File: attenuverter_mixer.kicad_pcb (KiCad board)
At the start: 2 copper layers, 98 parts, among them J0 Eurorack power, J1 Input, J10 Or out, J2 Out, J3 Input, J4 Out, J5 Input, J6 Input, J7 Out, J8 Out, J9 Sum out, U1 TL072, U2 TL072, U3 TL072, U4 TL072, U5 TL074, U6 LM4040CIZ-5.0

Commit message: Where it's at, just before changing the op amp configuration
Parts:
- removed D5, D6: D_TVS, Diode_THT:D_DO-15_P12.70mm_Horizontal
- removed R33, R36, R7, R8: 100R, Resistor_THT:R_Axial_DIN0204_L3.6mm_D1.6mm_P7.62mm_Horizontal
- J1, J10, J2, J3, J4, J5, J6, J7, J8, J9, RV1, RV2, RV3, RV4, RV5, RV6: moved to B.Cu
- R10, R11, R12, R13, R14, R15, R16, R17, R18, R19, R2, R20, R21, R22, R23, R24, R25, R26, R27, R28, R29, R3, R34, R35, R37, R38, R39, R4, R40, R41, R42, R45, R46, R6, R9: footprint Resistor_THT:R_Axial_DIN0207_L6.3mm_D2.5mm_P10.16mm_Horizontal -> Resistor_SMD:R_1206_3216Metric_Pad1.42x1.75mm_HandSolder
- moved J10 187.6 mm to (207.3, 134.9), turned to 270 degrees
- moved J8 184.8 mm to (224.5, 125.7)
- moved RV6 165.0 mm to (210.1, 122.7), turned to 90 degrees
- moved J9 152.4 mm to (190.8, 134.9), turned to 270 degrees
- moved J6 148.6 mm to (186.7, 125.2)
- moved D16 108.5 mm to (146.7, 82.7), turned to 180 degrees
- moved D17 100.8 mm to (130.9, 97.2)
- moved R30 94.9 mm to (153.0, 72.1), turned to 90 degrees
- moved R1 93.6 mm to (143.1, 73.0), turned to 90 degrees
- moved U5 90.7 mm to (168.1, 106.7), turned to 90 degrees
- moved U6 80.2 mm to (149.7, 121.3)
- moved C1 80.1 mm to (138.0, 102.6)
- moved J0 78.2 mm to (102.1, 110.5)
- moved R11 69.0 mm to (158.5, 59.7)
- moved C2 66.7 mm to (143.3, 115.7), turned to 180 degrees
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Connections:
- J0 pad 10: Net-(D16-Pad1) -> Net-(D17-Pad2)
- J0 pad 2: GND -> Net-(D16-Pad1)
- J0 pad 3: GNDPWR -> GND
- J0 pad 5: Net-(D17-Pad2) -> GNDPWR
- J0 pad 6: Net-(D17-Pad2) -> GNDPWR
- J0 pad 8: GNDPWR -> GND
- J0 pad 9: GND -> Net-(D17-Pad2)
- R15 pad 1: Net-(R15-Pad1) -> Net-(J1-PadT)
- R20 pad 2: Net-(R15-Pad1) -> Net-(J1-PadT)
- R21 pad 2: Net-(R21-Pad2) -> Net-(J3-PadT)
- R34 pad 1: Net-(D5-Pad1) -> Net-(J5-PadT)
- R37 pad 1: Net-(D6-Pad1) -> Net-(J6-PadT)
- R39 pad 2: Net-(D5-Pad1) -> Net-(J5-PadT)
- R40 pad 2: Net-(D6-Pad1) -> Net-(J6-PadT)
- R9 pad 1: Net-(R21-Pad2) -> Net-(J3-PadT)
- RV1 pad 1: Net-(R15-Pad1) -> Net-(J1-PadT)
- RV4 pad 1: Net-(R21-Pad2) -> Net-(J3-PadT)
- RV5 pad 1: Net-(D5-Pad1) -> Net-(J5-PadT)
- RV6 pad 1: Net-(D6-Pad1) -> Net-(J6-PadT)

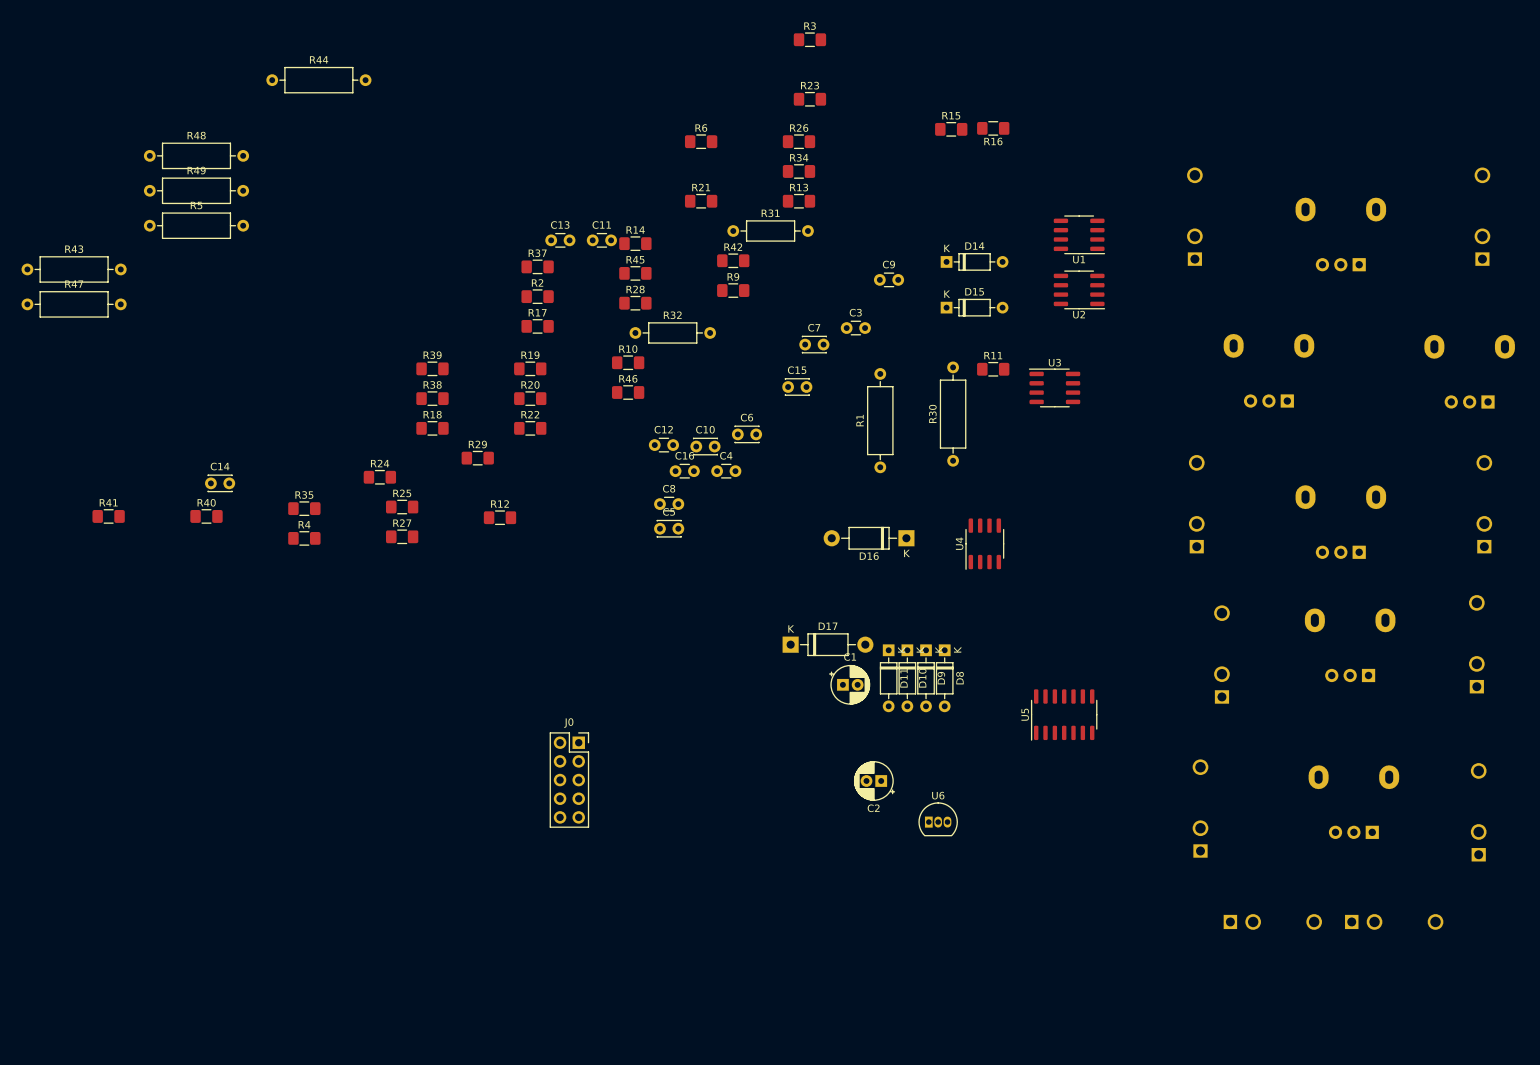
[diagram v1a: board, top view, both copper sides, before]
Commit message: V01 as fabricated
- Use surface mount 100K and 220K to allow single board.
- Drop offset pots --- just have atteunuvert controls on each channel.
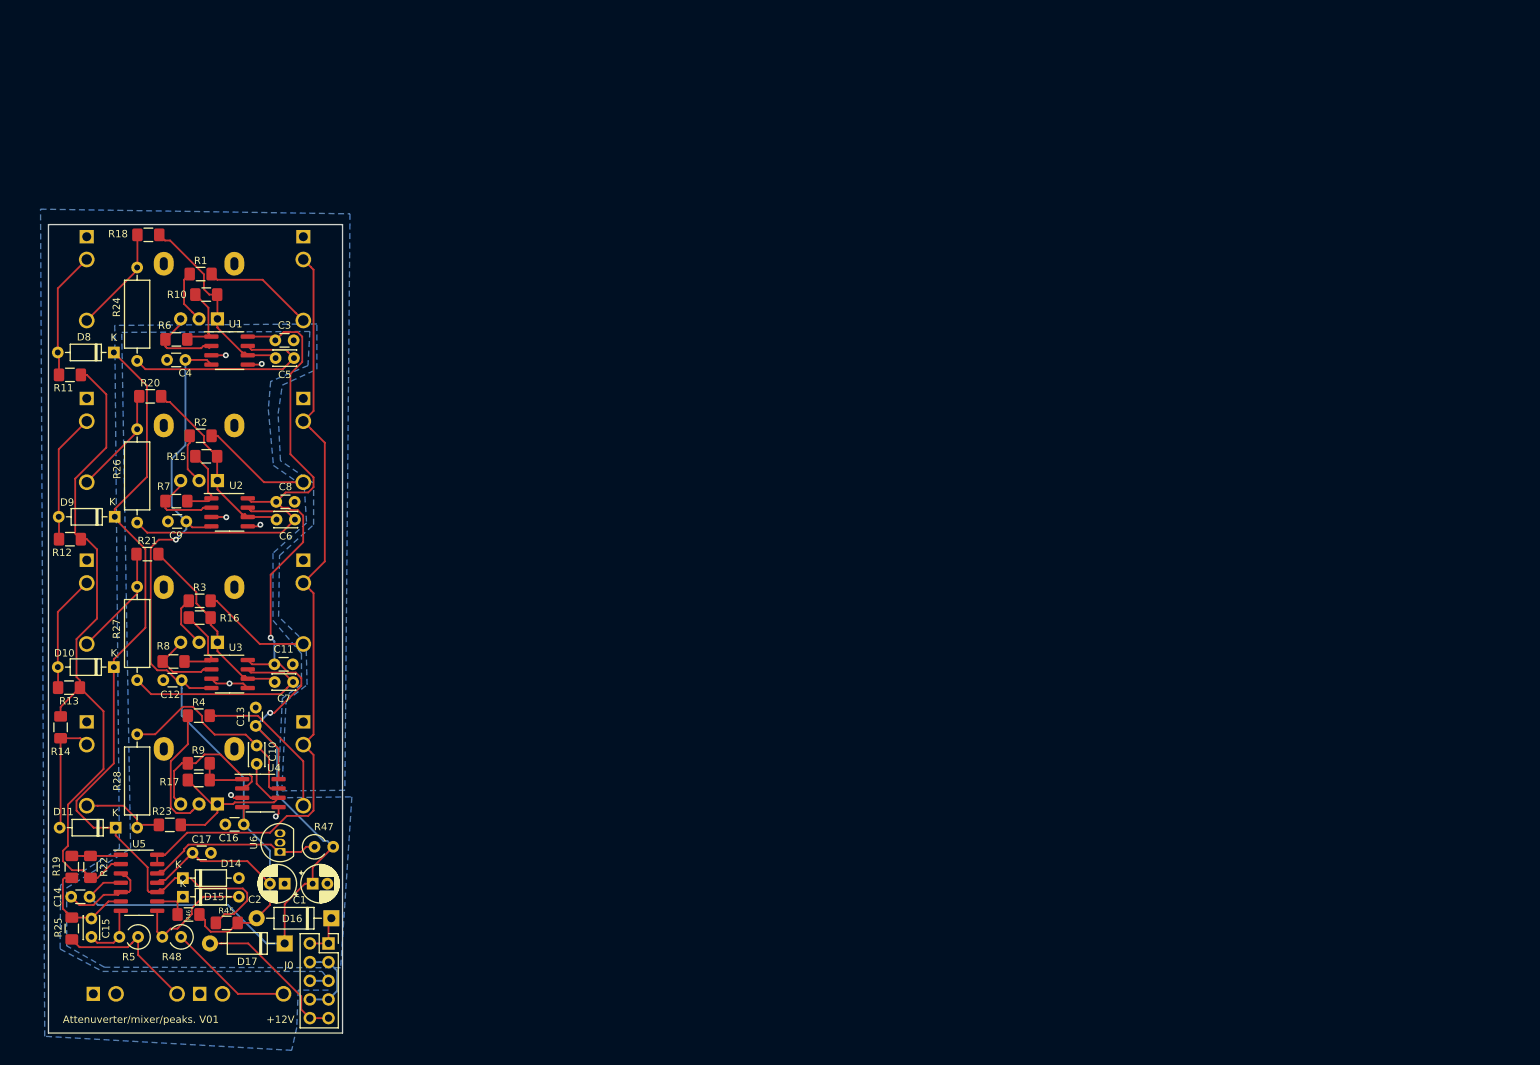
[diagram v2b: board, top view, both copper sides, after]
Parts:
- removed R29, R39, R40, R41, R42: 100k, Resistor_SMD:R_1206_3216Metric_Pad1.42x1.75mm_HandSolder
- removed R30, R43, R44: 330R, Resistor_THT:R_Axial_DIN0309_L9.0mm_D3.2mm_P12.70mm_Horizontal
- removed R31, R32: 100k, Resistor_THT:R_Axial_DIN0207_L6.3mm_D2.5mm_P10.16mm_Horizontal
- removed R34, R35, R37, R38: 47k, Resistor_SMD:R_1206_3216Metric_Pad1.42x1.75mm_HandSolder
- removed R49: R, Resistor_THT:R_Axial_DIN0309_L9.0mm_D3.2mm_P12.70mm_Horizontal
- removed RV5, RV6: 100k, Potentiometer_THT:Potentiometer_Alpha_RD901F-40-00D_Single_Vertical
- added C17: 100nF, Capacitor_THT:C_Disc_D3.0mm_W1.6mm_P2.50mm, F.Cu at (52.1, 125.5)
- added R7: 100k, Resistor_SMD:R_1206_3216Metric_Pad1.42x1.75mm_HandSolder, F.Cu at (47.4, 77.6)
- added R8: 100k, Resistor_SMD:R_1206_3216Metric_Pad1.42x1.75mm_HandSolder, F.Cu at (47.0, 99.4)
- C14: value 18pF -> 100nF; footprint Capacitor_THT:C_Disc_D3.0mm_W2.0mm_P2.50mm -> Capacitor_THT:C_Disc_D3.0mm_W1.6mm_P2.50mm
- J4: value Out -> Input
- J6: value Input -> Out
- R1: value 330R -> 100k; footprint Resistor_THT:R_Axial_DIN0309_L9.0mm_D3.2mm_P12.70mm_Horizontal -> Resistor_SMD:R_1206_3216Metric_Pad1.42x1.75mm_HandSolder
- R10, R15, R16, R9: value 47k -> 100k
- R24, R26, R27, R28: value 100k -> 330R; footprint Resistor_SMD:R_1206_3216Metric_Pad1.42x1.75mm_HandSolder -> Resistor_THT:R_Axial_DIN0309_L9.0mm_D3.2mm_P12.70mm_Horizontal
- R47, R48, R5: footprint Resistor_THT:R_Axial_DIN0309_L9.0mm_D3.2mm_P12.70mm_Horizontal -> Resistor_THT:R_Axial_DIN0309_L9.0mm_D3.2mm_P2.54mm_Vertical
- RV1, RV2, RV3, RV4: value 100k -> 10k
- moved J8 190.2 mm to (35.2, 107.7), turned to 180 degrees
- moved J2 189.9 mm to (35.2, 41.7), turned to 180 degrees
- moved J7 189.9 mm to (35.2, 85.7), turned to 180 degrees
- moved RV3 175.9 mm to (53.0, 96.8)
- moved J6 163.5 mm to (35.2, 63.7), turned to 180 degrees
- moved J4 160.7 mm to (64.6, 85.7), turned to 180 degrees
- moved RV4 159.1 mm to (53.0, 118.8)
- moved J10 157.0 mm to (50.5, 144.7)
- moved RV1 155.5 mm to (53.0, 52.8)
- moved J9 155.0 mm to (36.1, 144.7)
- moved RV2 145.9 mm to (53.0, 74.8)
- moved D14 133.5 mm to (48.3, 128.9)
- moved R23 131.6 mm to (46.5, 121.7)
- moved D15 131.2 mm to (48.3, 131.4)
- moved U5 127.9 mm to (42.3, 129.5), turned to 0 degrees
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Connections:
- C14 pad 1: Net-(C14-Pad1) -> +12V
- C14 pad 2: Net-(C14-Pad2) -> GND
- J1 pad TN: GND -> /Vref
- J3 pad TN: GND -> /Vref
- J4 pad TN: /out_2 -> /Vref
- J6 pad TN: /Vref -> /out_2
- R1 pad 1: Net-(J2-PadT) -> Net-(R1-Pad1)
- R1 pad 2: Net-(R1-Pad2) -> Net-(J1-PadT)
- R10 pad 1: GND -> Net-(C5-Pad2)
- R11 pad 1: Net-(C14-Pad2) -> Net-(R11-Pad1)
- R12 pad 1: Net-(C14-Pad2) -> Net-(R11-Pad1)
- R13 pad 1: Net-(C14-Pad2) -> Net-(R11-Pad1)
- R14 pad 1: Net-(C14-Pad2) -> Net-(R11-Pad1)
- R15 pad 1: Net-(J1-PadT) -> Net-(C6-Pad2)
- R16 pad 1: GND -> Net-(C7-Pad2)
- R16 pad 2: Net-(R15-Pad2) -> Net-(R16-Pad2)
- R17 pad 1: Net-(R17-Pad1) -> Net-(C10-Pad2)
- R18 pad 1: Net-(R18-Pad1) -> Net-(J2-PadT)
- R18 pad 2: Net-(R18-Pad2) -> Net-(C5-Pad2)
- R19 pad 1: Net-(C14-Pad1) -> Net-(R19-Pad1)
- R2 pad 2: /Vref -> Net-(J3-PadT)
- R20 pad 1: Net-(C10-Pad1) -> Net-(J6-PadT)
- R20 pad 2: Net-(J1-PadT) -> Net-(C6-Pad2)
- R21 pad 1: Net-(C5-Pad1) -> Net-(J7-PadT)
- R21 pad 2: Net-(J3-PadT) -> Net-(C7-Pad2)
- R22 pad 1: Net-(C14-Pad1) -> Net-(R19-Pad1)
- R22 pad 2: Net-(C14-Pad2) -> Net-(R11-Pad1)
- R23 pad 1: Net-(C10-Pad2) -> Net-(J8-PadT)
- R23 pad 2: Net-(C10-Pad1) -> Net-(C10-Pad2)
- R24 pad 1: Net-(R17-Pad1) -> Net-(J2-PadT)
- R24 pad 2: Net-(C10-Pad2) -> Net-(C5-Pad1)
- R25 pad 1: Net-(C15-Pad1) -> Net-(C15-Pad2)
- R25 pad 2: Net-(C15-Pad2) -> Net-(J9-PadT)
- R26 pad 1: Net-(C5-Pad2) -> Net-(J6-PadT)
- R26 pad 2: Net-(C5-Pad1) -> Net-(C6-Pad1)
- R27 pad 1: Net-(R18-Pad1) -> Net-(J7-PadT)
- R27 pad 2: Net-(C5-Pad2) -> Net-(C7-Pad1)
- R28 pad 1: Net-(R28-Pad1) -> Net-(J8-PadT)
- R28 pad 2: Net-(R1-Pad2) -> Net-(C10-Pad1)
- R3 pad 2: /Vref -> Net-(J4-PadT)
- R4 pad 1: Net-(R2-Pad1) -> Net-(R4-Pad1)
- R4 pad 2: Net-(R17-Pad2) -> Net-(J5-PadT)
- R6 pad 1: Net-(R3-Pad1) -> Net-(R10-Pad2)
- R6 pad 2: Net-(R18-Pad2) -> Net-(R6-Pad2)
- R9 pad 1: Net-(J3-PadT) -> Net-(R17-Pad2)
- R9 pad 2: Net-(R10-Pad2) -> Net-(R9-Pad2)
- RV1 pad 1: Net-(J1-PadT) -> Net-(C5-Pad2)
- RV1 pad 2: Net-(R15-Pad2) -> Net-(R1-Pad1)
- RV1 pad 3: GND -> Net-(R6-Pad2)
- RV2 pad 1: /Vref -> Net-(C6-Pad2)
- RV2 pad 2: Net-(RV2-Pad2) -> Net-(R2-Pad1)
- RV2 pad 3: GND -> Net-(R7-Pad2)
- RV3 pad 1: /Vref -> Net-(C7-Pad2)
- RV3 pad 2: Net-(RV3-Pad2) -> Net-(R3-Pad1)
- RV3 pad 3: GND -> Net-(R8-Pad2)
- RV4 pad 1: Net-(J3-PadT) -> Net-(C10-Pad2)
- RV4 pad 2: Net-(R10-Pad2) -> Net-(R4-Pad1)
- RV4 pad 3: GND -> Net-(R9-Pad2)
- U1 pad 1: Net-(C10-Pad2) -> Net-(R10-Pad2)
- U1 pad 2: Net-(C10-Pad1) -> Net-(R6-Pad2)
- U1 pad 3: Net-(R15-Pad2) -> GND
- U1 pad 5: Net-(RV2-Pad2) -> GND
- U1 pad 6: Net-(R2-Pad1) -> Net-(C5-Pad2)
- U1 pad 7: Net-(R17-Pad2) -> Net-(C5-Pad1)
- U2 pad 1: Net-(R1-Pad2) -> Net-(R15-Pad2)
- U2 pad 2: Net-(R28-Pad1) -> Net-(R7-Pad2)
- U2 pad 3: Net-(R17-Pad1) -> GND
- U2 pad 5: Net-(R18-Pad1) -> GND
- U2 pad 6: Net-(R29-Pad1) -> Net-(C6-Pad2)
- U2 pad 7: Net-(R29-Pad2) -> Net-(C6-Pad1)
- U3 pad 1: Net-(C5-Pad2) -> Net-(R16-Pad2)
- U3 pad 2: Net-(C5-Pad1) -> Net-(R8-Pad2)
- U3 pad 3: Net-(R10-Pad2) -> GND
- U3 pad 5: Net-(RV3-Pad2) -> GND
- U3 pad 6: Net-(R3-Pad1) -> Net-(C7-Pad2)
- U3 pad 7: Net-(R18-Pad2) -> Net-(C7-Pad1)
- U4 pad 1: Net-(C6-Pad2) -> Net-(R17-Pad2)
- U4 pad 2: Net-(C6-Pad1) -> Net-(R9-Pad2)
- U4 pad 3: Net-(R34-Pad2) -> GND
- U4 pad 5: Net-(R37-Pad2) -> GND
- U4 pad 6: Net-(C7-Pad1) -> Net-(C10-Pad2)
- U4 pad 7: Net-(C7-Pad2) -> Net-(C10-Pad1)
- U5 pad 1: Net-(C14-Pad1) -> Net-(R19-Pad1)
- U5 pad 12: GND -> Net-(R47-Pad1)
- U5 pad 13: Net-(U5-Pad13) -> /Vref
- U5 pad 14: Net-(U5-Pad13) -> /Vref
- U5 pad 2: Net-(C14-Pad2) -> Net-(R11-Pad1)
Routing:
- net +12V: track 0.00 -> 165.7 mm, vias 0 -> 2
- net -12V: track 0.00 -> 133.2 mm, vias 0 -> 1
- net Net-(D10-Pad1): track 0.00 -> 110.1 mm
- net /Vref: track 0.00 -> 105.3 mm
- net Net-(R11-Pad1): track 0.00 -> 91.1 mm
- net GND: track 0.00 -> 39.9 mm, vias 0 -> 7
- net Net-(C6-Pad1): track 0.00 -> 29.9 mm
- net Net-(C7-Pad1): track 0.00 -> 29.6 mm
- net Net-(C5-Pad1): track 0.00 -> 29.4 mm
- net Net-(C10-Pad1): track 0.00 -> 28.2 mm
- net Net-(C10-Pad2): track 0.00 -> 27.4 mm
- net Net-(C5-Pad2): track 0.00 -> 26.6 mm
- net Net-(C7-Pad2): track 0.00 -> 26.1 mm
- net Net-(C6-Pad2): track 0.00 -> 25.8 mm
- net Net-(R47-Pad1): track 0.00 -> 23.9 mm
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- added copper zone on B.Cu, net GND
- added copper zone on B.Cu, net GNDPWR
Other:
- board outline added: 40 x 110 mm
- board text added: "+12V"
- board text added: "Attenuverter/mixer/peaks. V01"
